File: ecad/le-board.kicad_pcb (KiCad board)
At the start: 2 copper layers, 262.2 x 79.8 mm, 88 parts

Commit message: chore: pcb update
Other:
- board text removed: "Break lines"

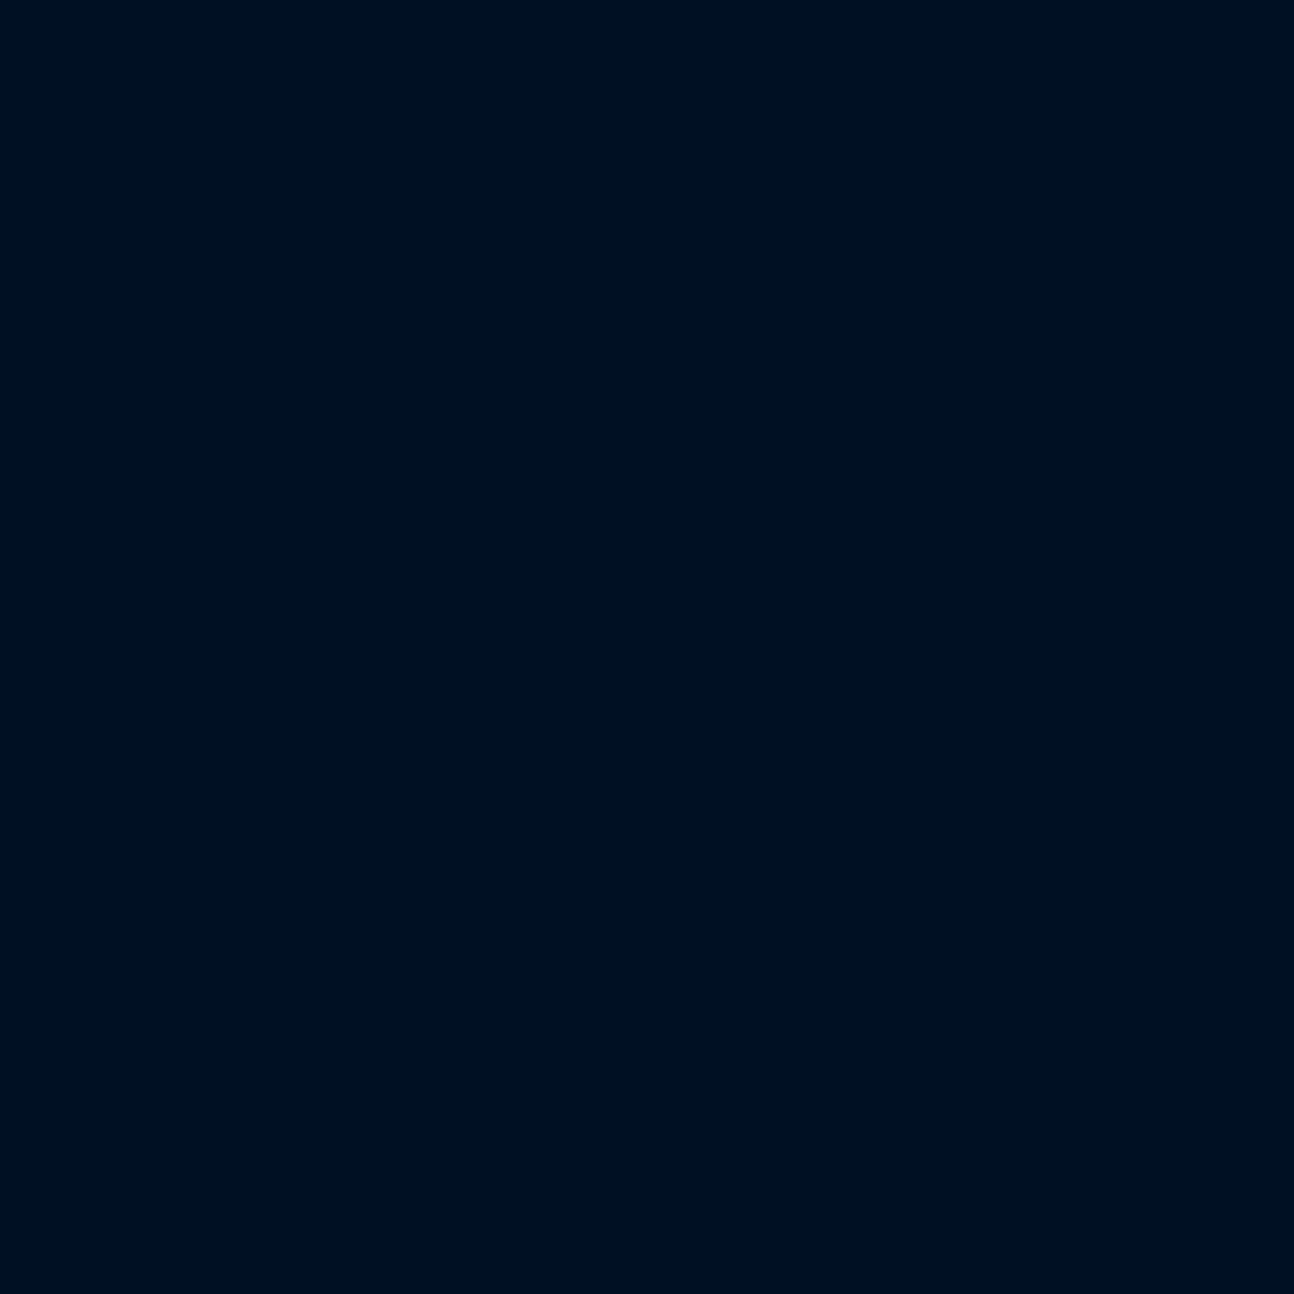
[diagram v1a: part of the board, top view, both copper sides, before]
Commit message: feat: wave coil script
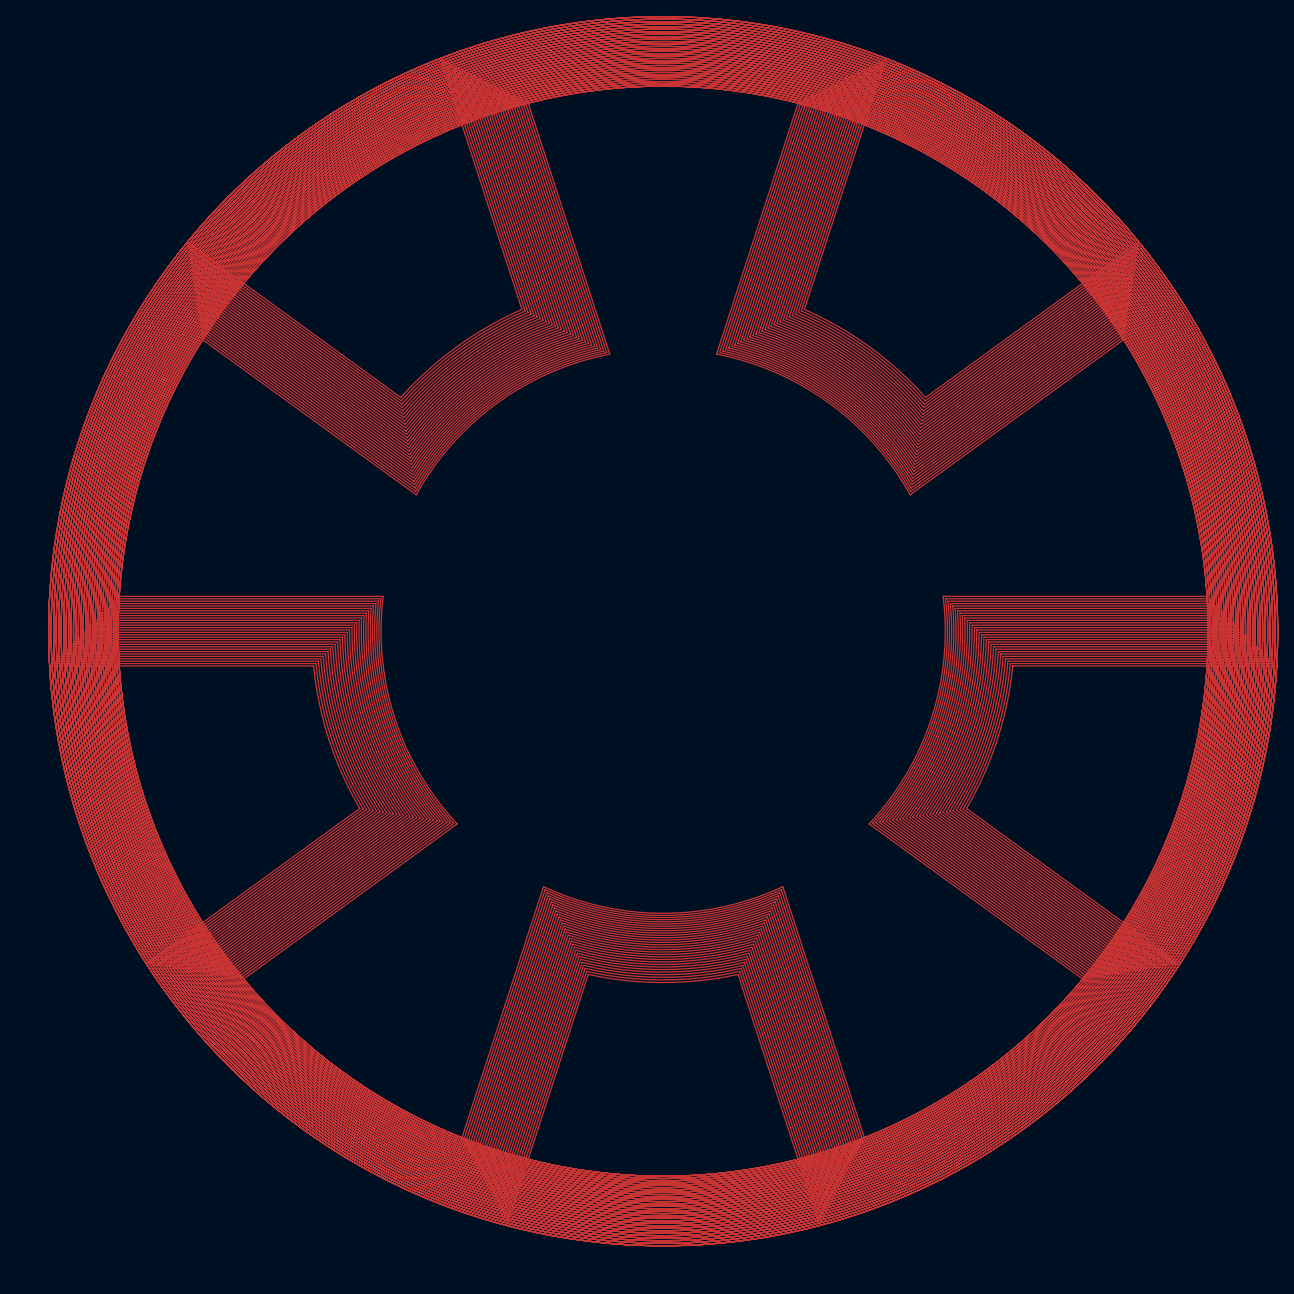
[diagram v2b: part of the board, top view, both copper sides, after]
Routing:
- net (no net): track 0.00 -> 24202.0 mm

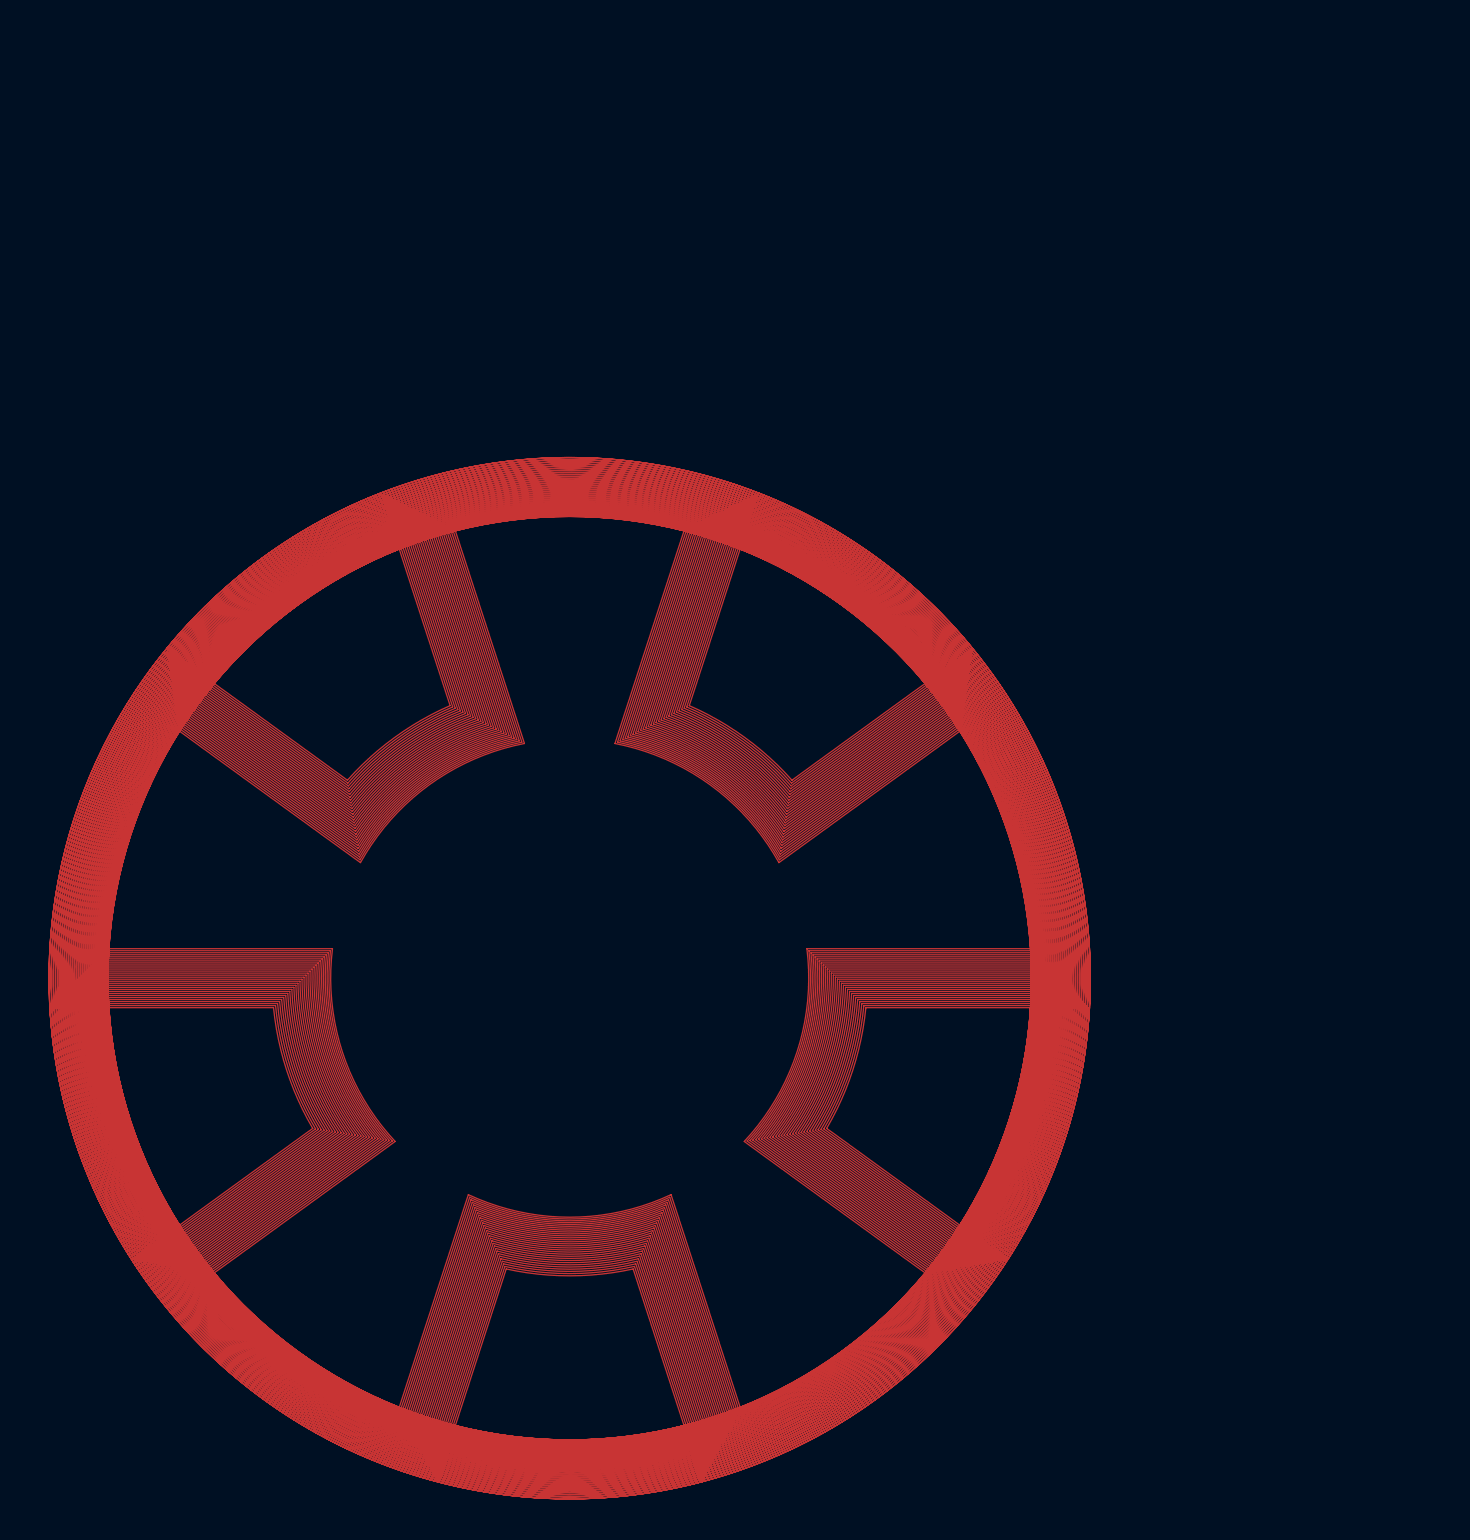
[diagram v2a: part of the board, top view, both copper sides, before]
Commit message: chore: generated PCB stator
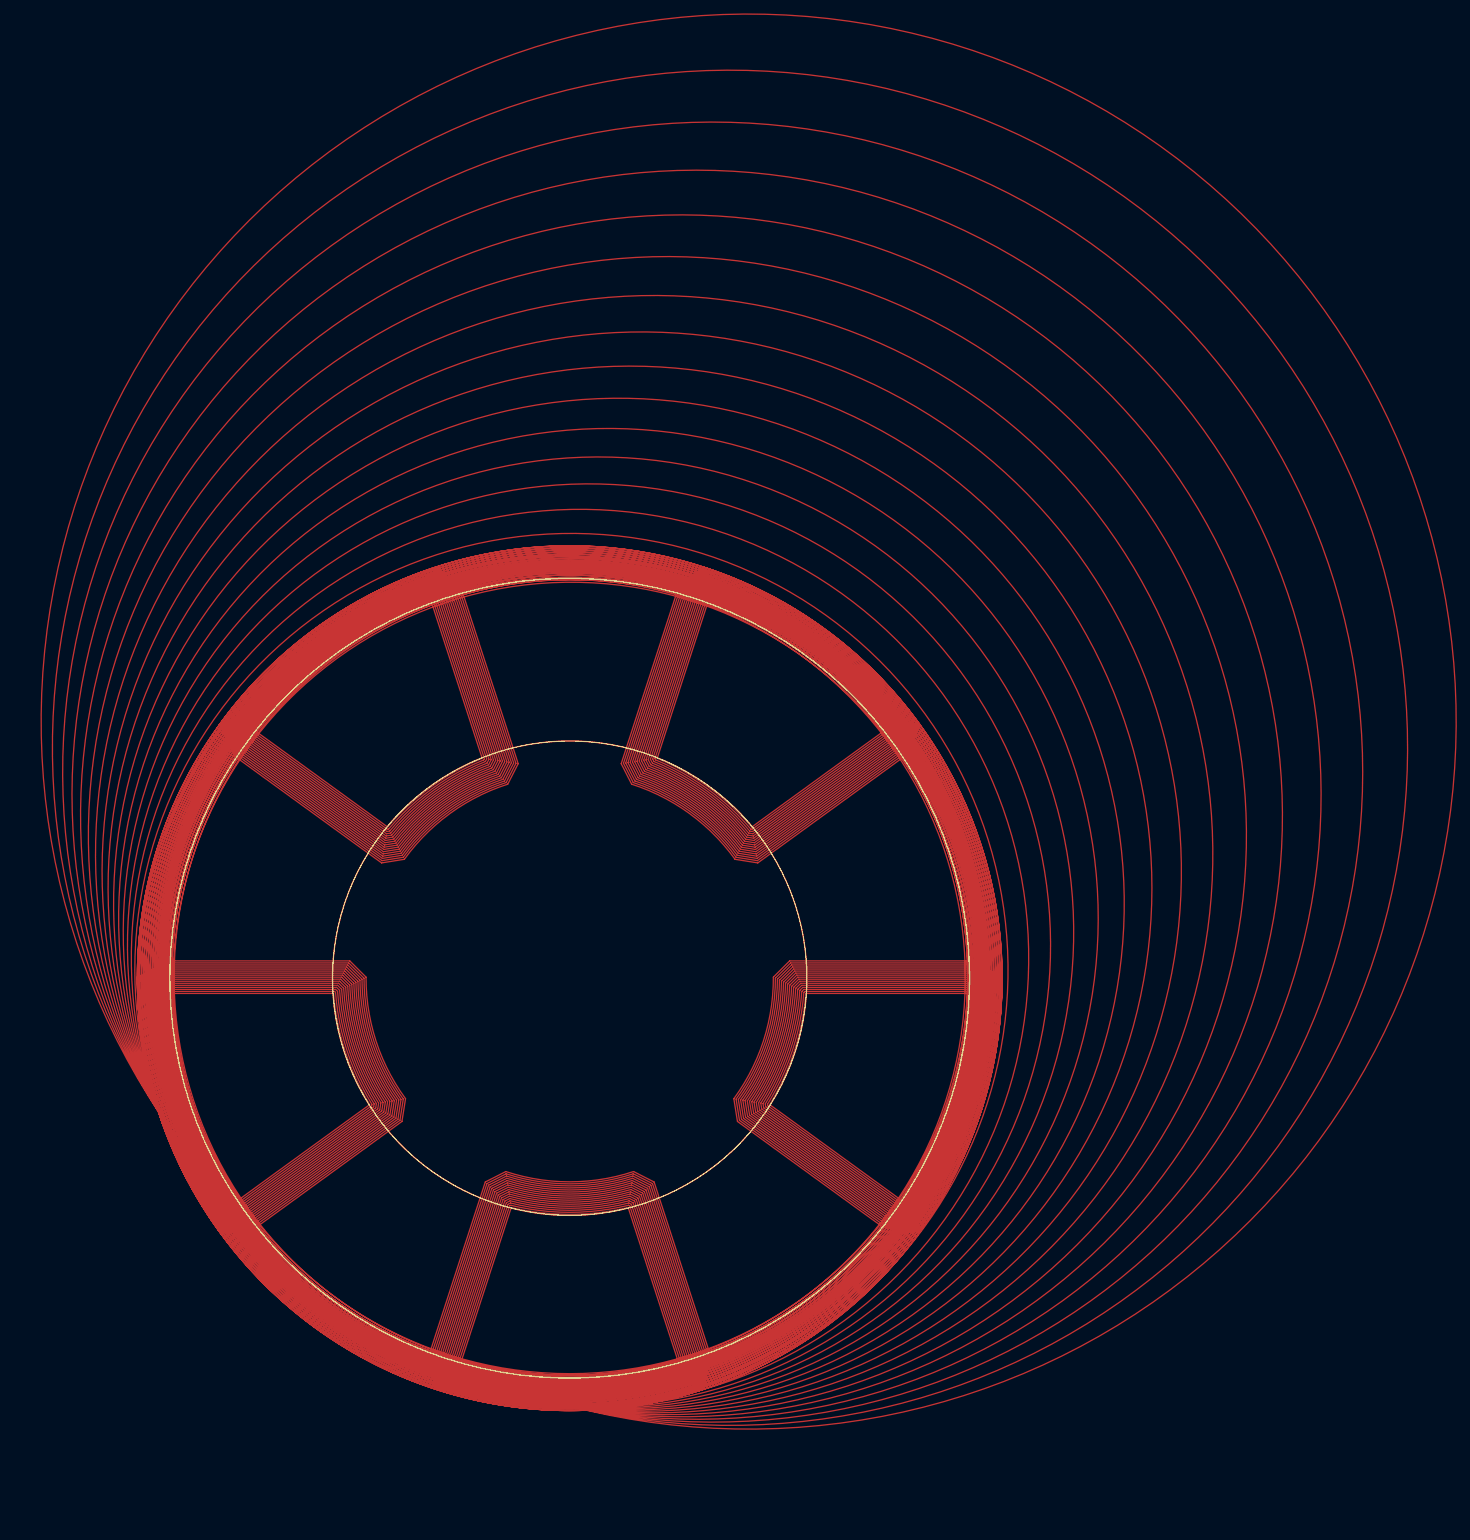
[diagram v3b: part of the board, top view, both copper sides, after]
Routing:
- net (no net): track 24202.0 -> 38917.6 mm
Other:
- copper layers 2 -> 4

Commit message: chore: wave coils
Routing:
- net (no net): track 38917.6 -> 43844.8 mm
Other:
- board size 262.2 x 79.8 mm -> 425.8 x 88.4 mm

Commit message: chore: PCB cut edge updates
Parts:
- moved MX11 67.9 mm to (325.0, 37.5)
- moved MX23 67.9 mm to (325.0, 56.7)
- moved MX35 67.9 mm to (325.0, 75.9)
- moved D10 67.9 mm to (310.9, 40.5)
- moved D22 67.9 mm to (310.9, 59.7)
- moved D34 67.9 mm to (310.9, 78.9)
- moved D44 67.9 mm to (310.9, 98.1)
- moved MX19 67.9 mm to (248.2, 56.7)
- moved MX31 67.9 mm to (248.2, 75.9)
- moved MX41 67.9 mm to (248.2, 95.1)
- moved MX7 67.9 mm to (248.2, 37.5)
- moved D11 67.9 mm to (330.1, 40.5)
- moved D12 67.9 mm to (349.3, 40.5)
- moved D19 67.9 mm to (253.3, 59.7)
- moved D20 67.9 mm to (272.5, 59.7)
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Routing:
- net (no net): track 43844.8 -> 21873.5 mm
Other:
- board size 425.8 x 88.4 mm -> 291 x 252.6 mm
